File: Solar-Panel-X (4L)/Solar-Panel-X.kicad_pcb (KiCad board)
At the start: 4 copper layers, 48.4 x 48.4 mm, 81 parts, among them J1 FTS-105-01-L-DV-A, Q1 BSS138DWQ-7, Q2 MBT2222ADW1T1, Q3 BSS138DWQ-7, Q4 MBT2222ADW1T1, U1 BQ25570RGRR, U2 TSL2561

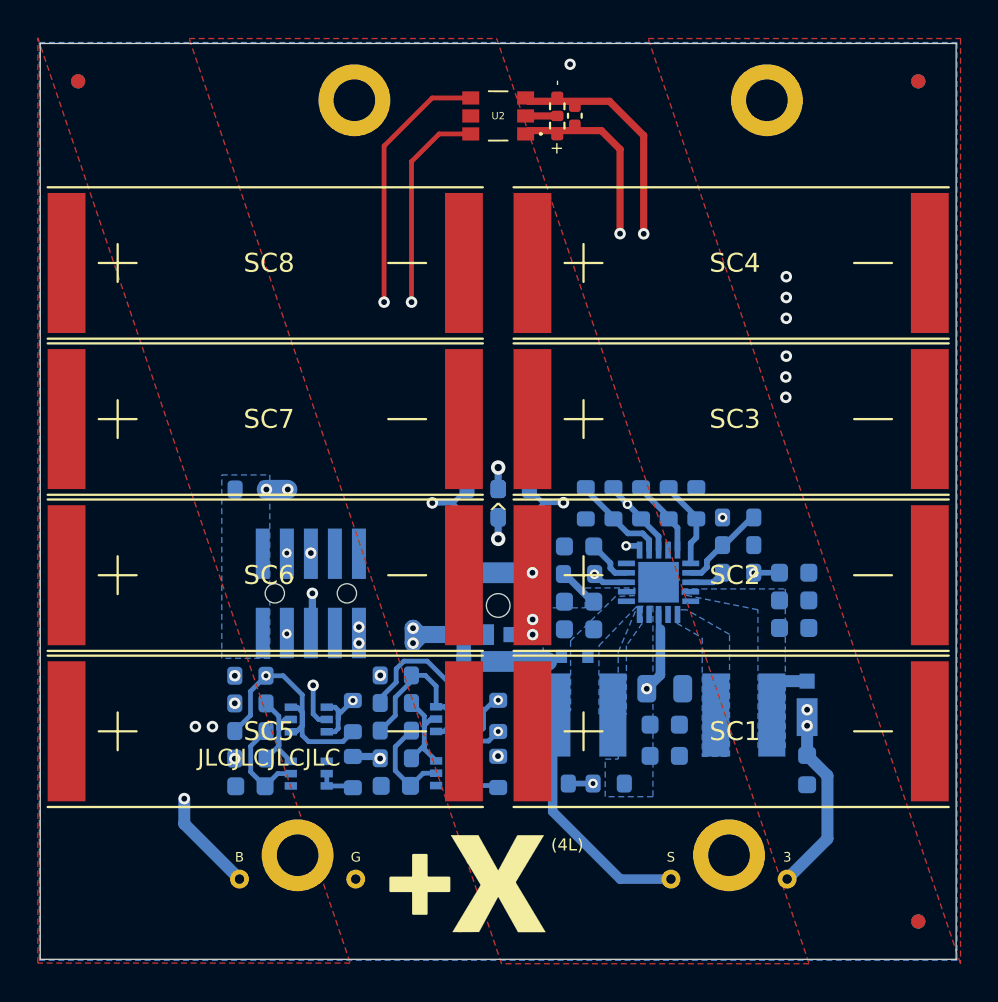
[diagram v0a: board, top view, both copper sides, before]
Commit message: DFM updates and repositioned -Z mounting holes
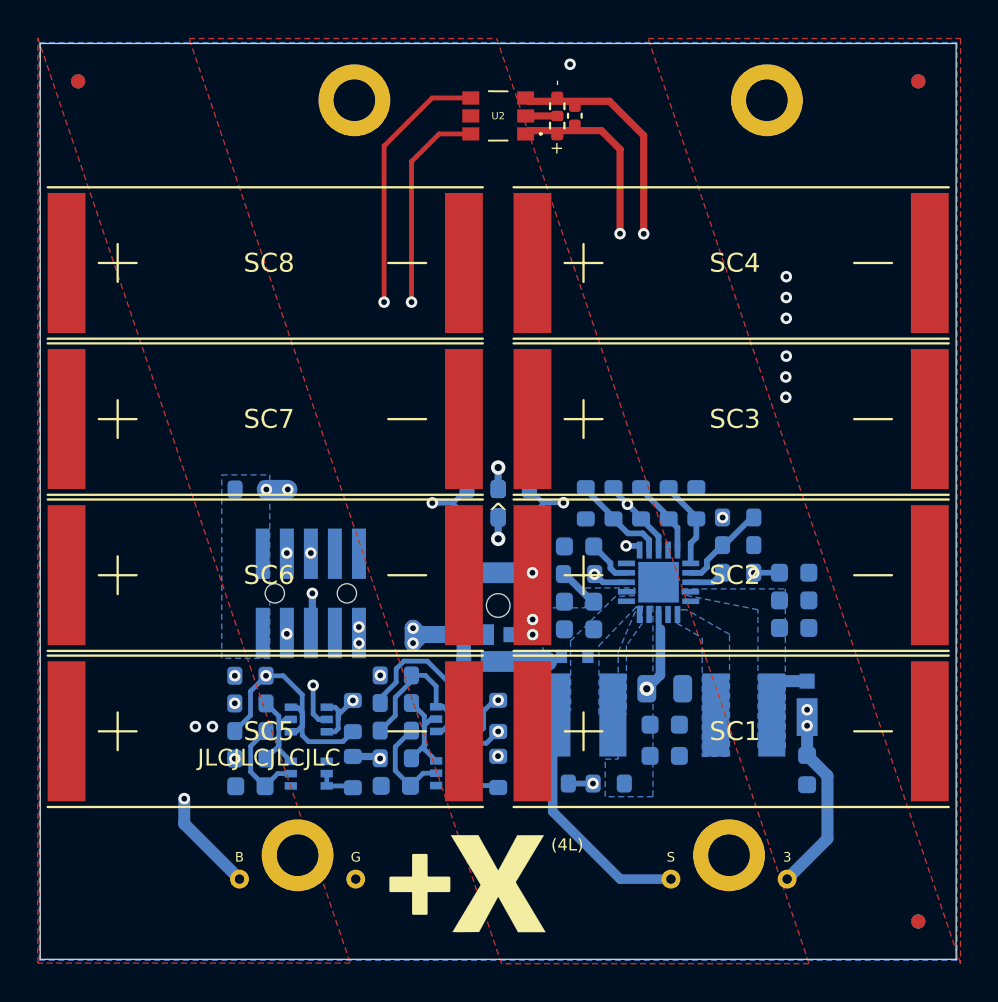
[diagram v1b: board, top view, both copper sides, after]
